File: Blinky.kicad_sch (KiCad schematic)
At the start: 34 parts, among them J1 DTF13-4P-G003, J2 Conn_01x01, J3 Conn_01x01, J4 Conn_01x01, Q1 IPD90P03P404ATMA2, Q2 IPD90P03P404ATMA2, U1 DCM4623TD2J13D0T70, U2 LTC3638xMSE

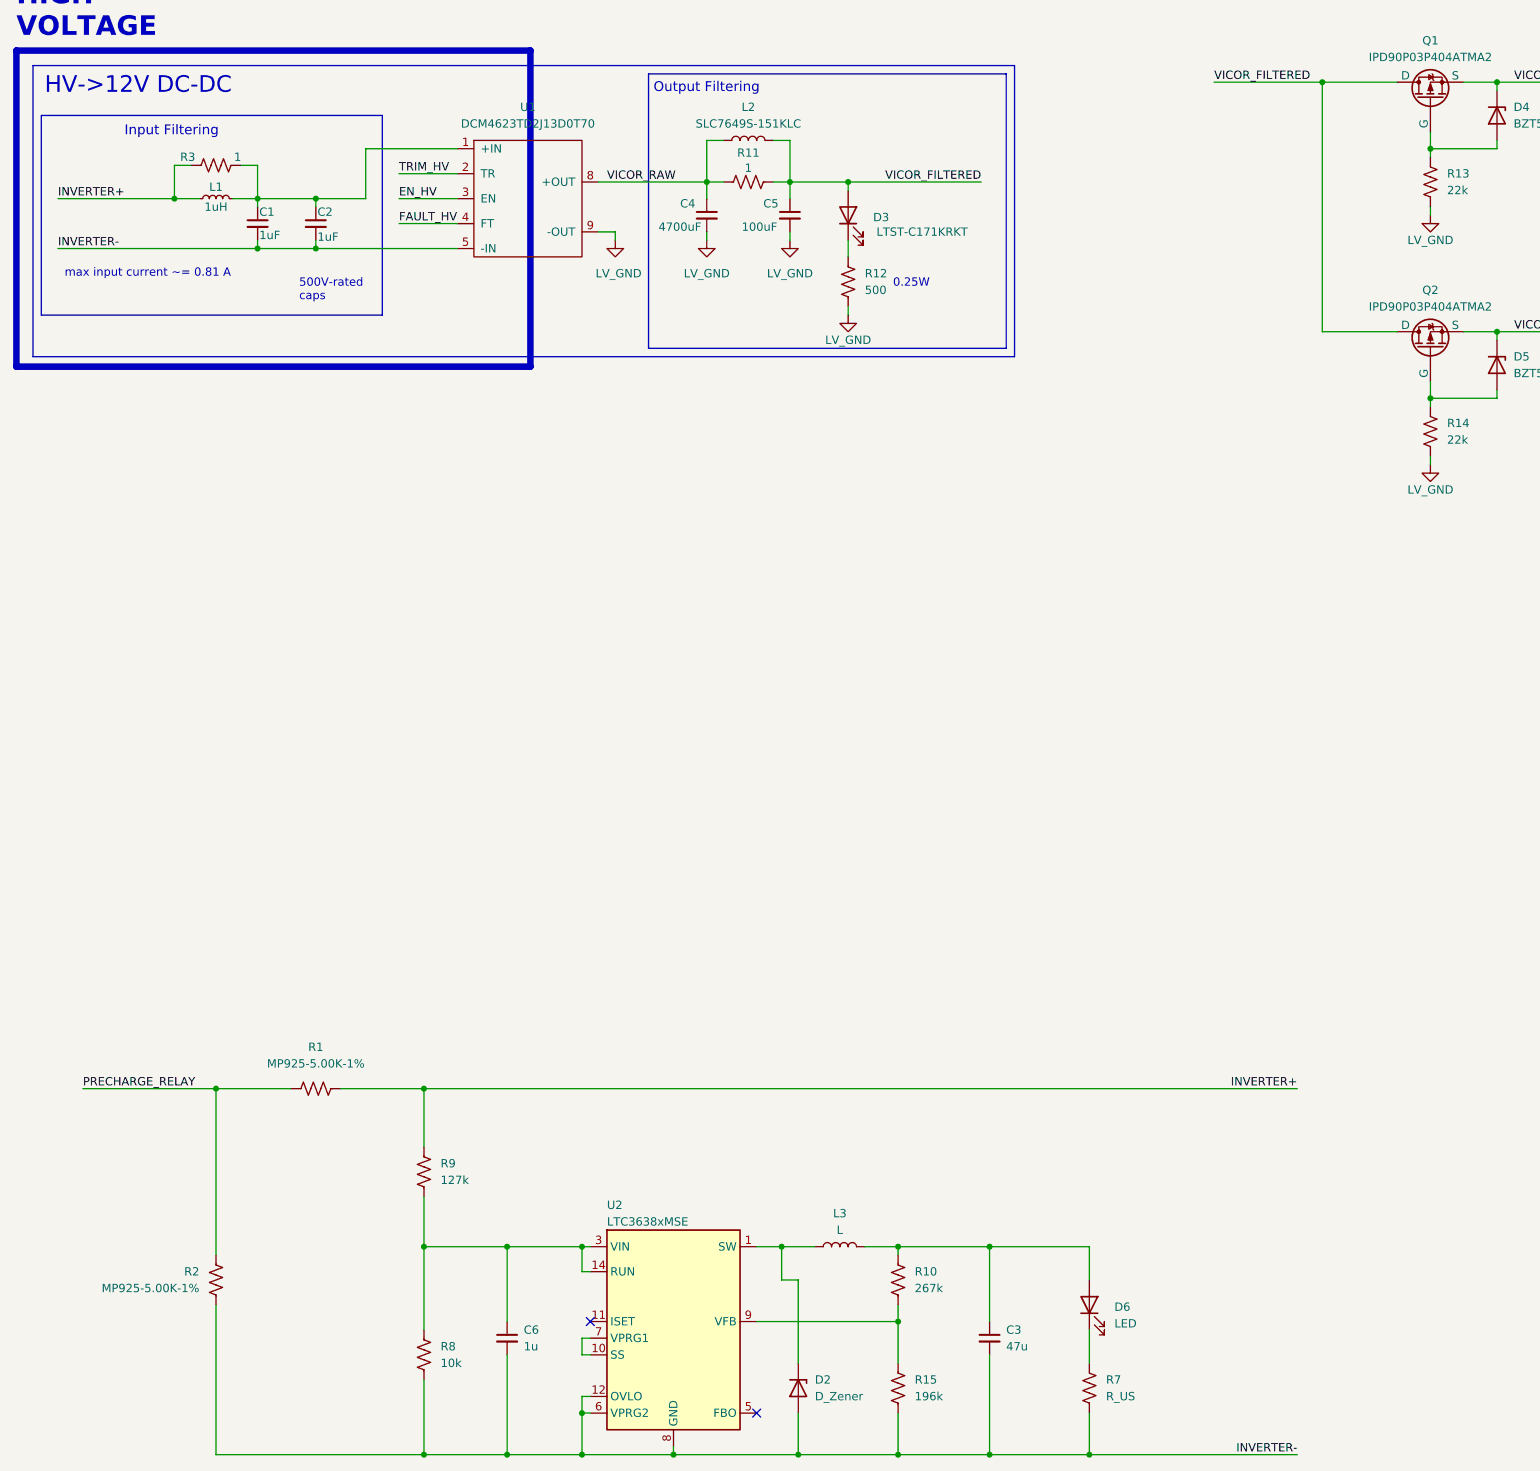
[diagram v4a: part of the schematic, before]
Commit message: further adjusted buck schematic
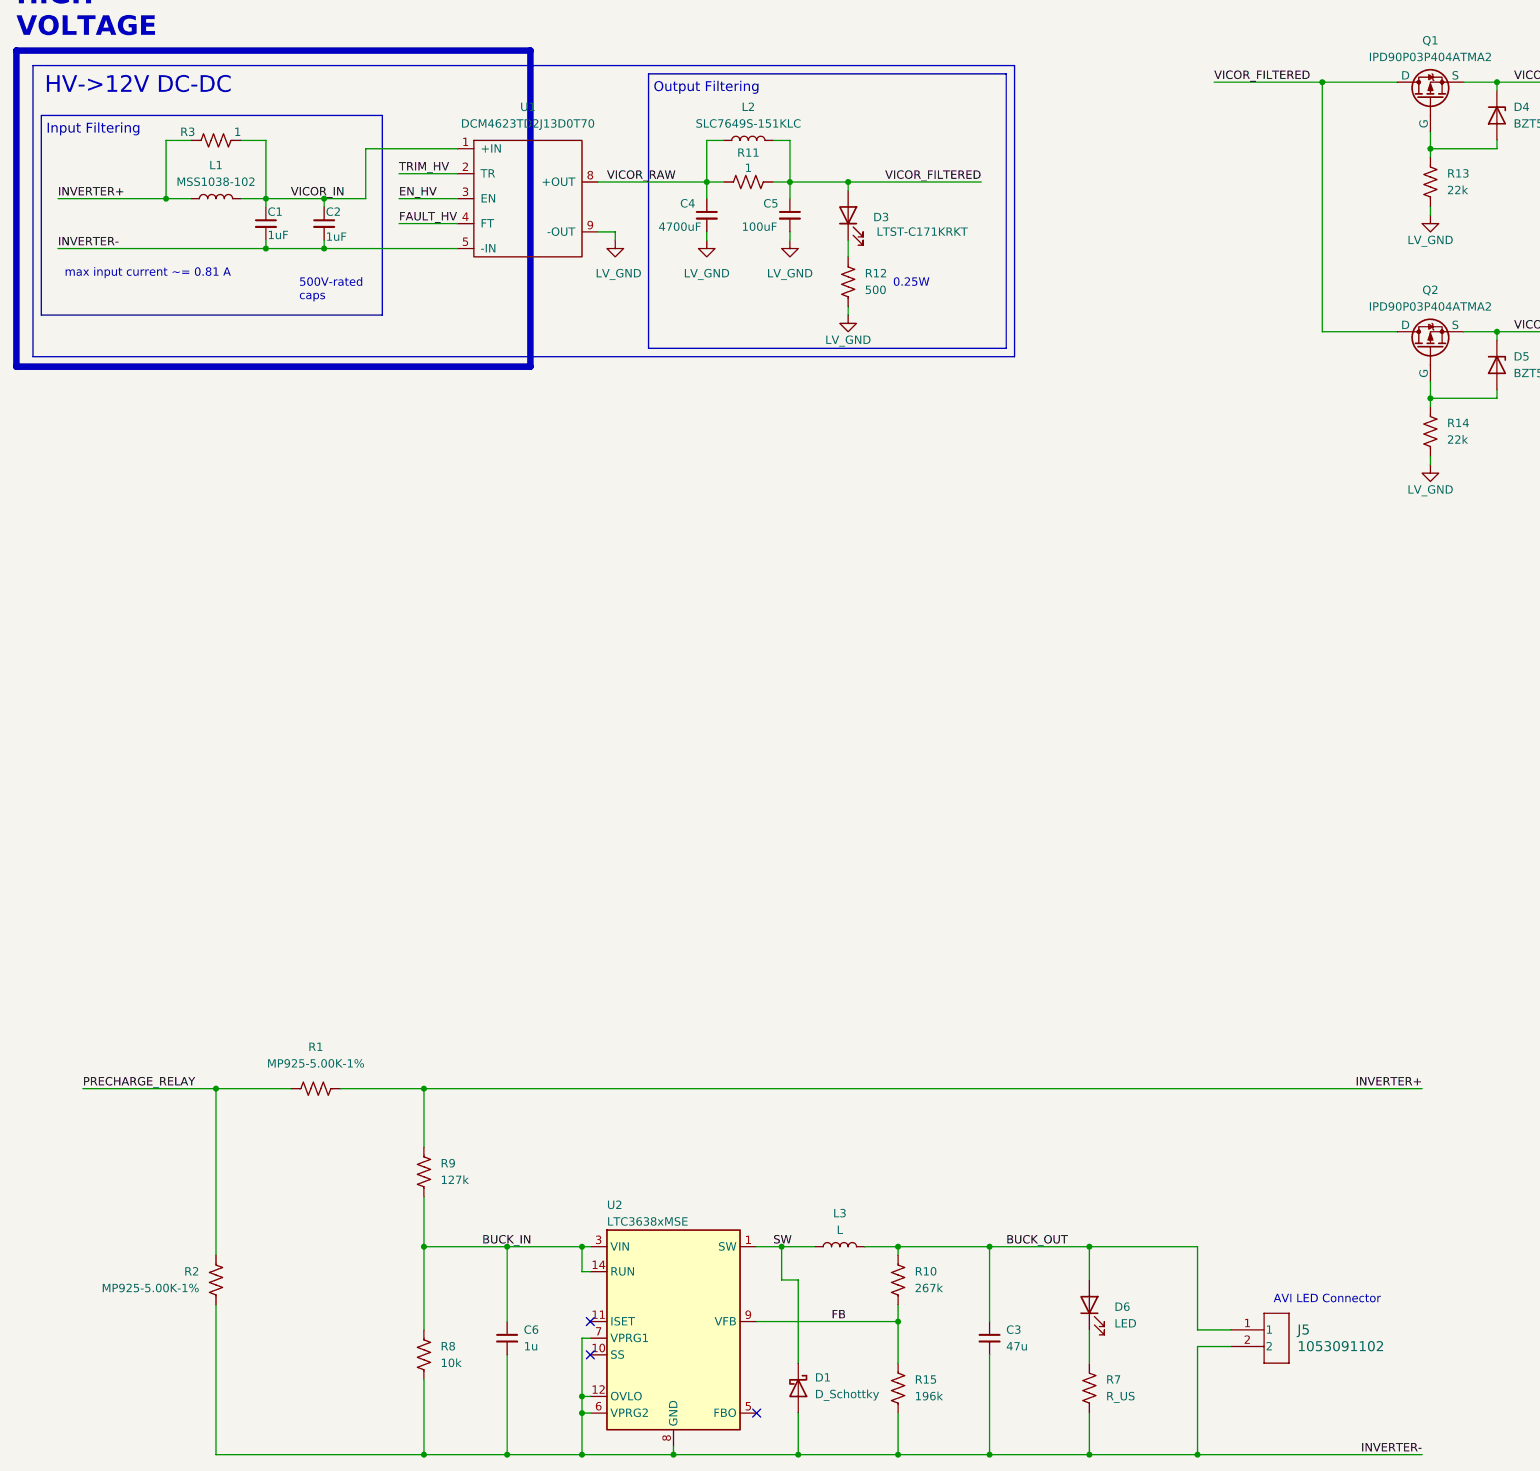
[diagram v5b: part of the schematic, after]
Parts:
- removed D2: D_Zener, symbol Device:D_Zener
- removed L1: 1uH, Inductor_SMD:L_1008_2520Metric_Pad1.43x2.20mm_HandSolder, symbol Device:L_Small
- added D1: D_Schottky, symbol Device:D_Schottky
- added J5: 1053091102, AERO_Connectors:1053091102, symbol AERO_Connectors:1053091102
- added L1: MSS1038-102, AERO_Inductors:MSS1038-102, symbol AERO_Inductors:MSS1038-102
- D6: footprint (none) -> LED_SMD:LED_0805_2012Metric_Pad1.15x1.40mm_HandSolder
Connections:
- net INVERTER+: now also L1.1
- net INVERTER-: now also U2.7 (VPRG1), D1.2 (A), J5.2
- net BUCK_IN: now reaches C6.1, R8.1, R9.2, U2.14 (RUN), U2.3 (VIN)
- net SW: now reaches L3.1, U2.1 (SW)
- net SW: now also D1.1 (K)
- net at U2.10 (SS): no longer U2.7 (VPRG1)
- net FB: now reaches R10.2, R15.1, U2.9 (VFB)
- net VICOR_IN: now reaches C1.1, C2.1, R3.1, U1.1 (+IN)
- net VICOR_IN: now also L1.2
- net BUCK_OUT: now reaches C3.1, D6.2 (A), L3.2, R10.1
- net BUCK_OUT: now also J5.1
- no-connect marks 2 -> 3
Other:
- note added: "AVI LED Connector"
- moved on the sheet: C1, C2, R3

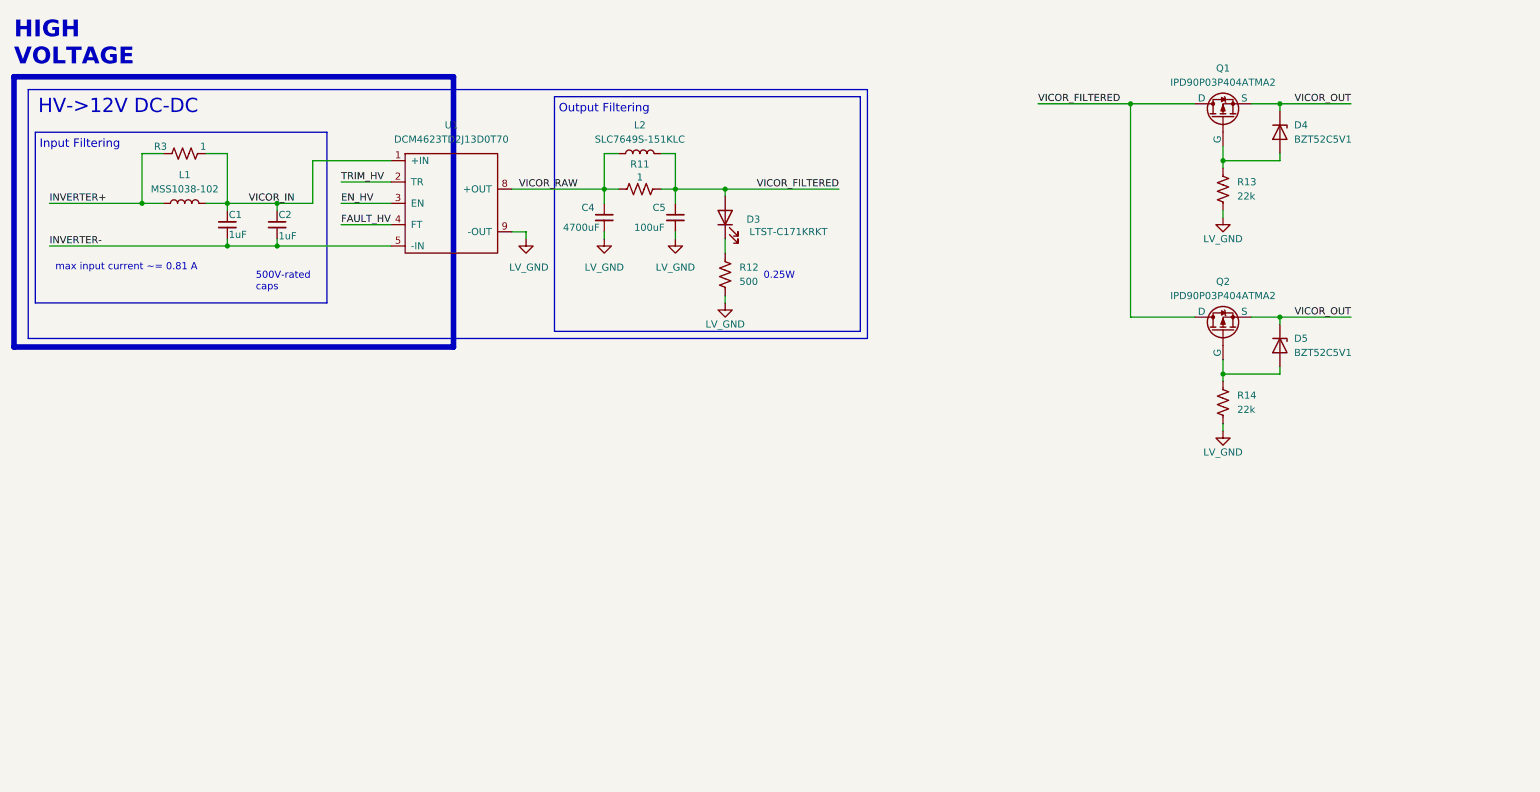
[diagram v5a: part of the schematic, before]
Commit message: added second VICOR
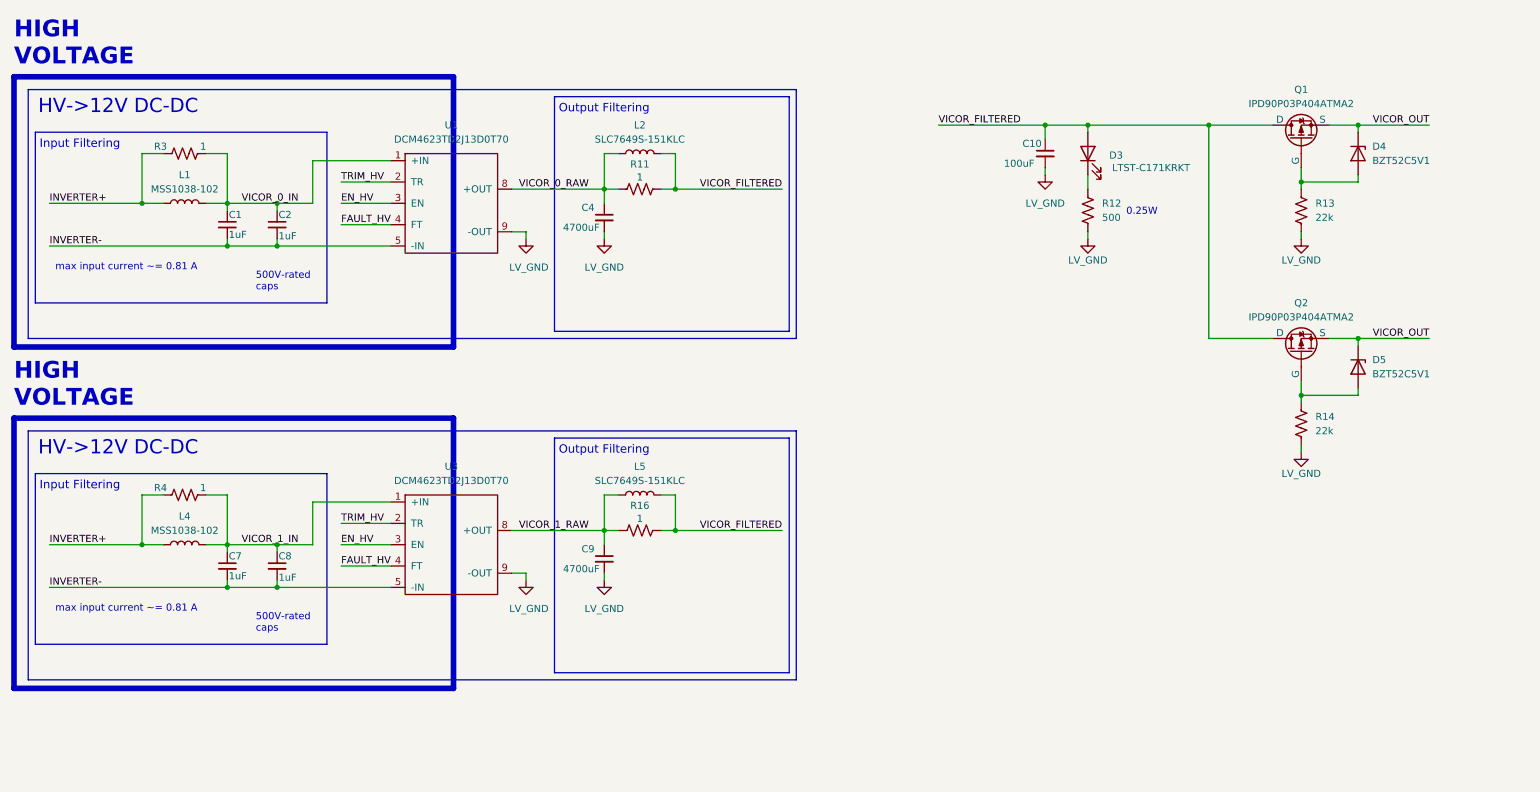
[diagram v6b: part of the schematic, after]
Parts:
- removed C5: 100uF, Capacitor_THT:C_Radial_D12.5mm_H25.0mm_P5.00mm, symbol Device:C_Small
- added C10: 100uF, Capacitor_THT:C_Radial_D12.5mm_H25.0mm_P5.00mm, symbol Device:C_Small
- added C7, C8: 1uF, Capacitor_THT:C_Rect_L18.0mm_W8.0mm_P15.00mm_FKS3_FKP3, symbol Device:C_Small
- added C9: 4700uF, Capacitor_THT:C_Radial_D12.5mm_H25.0mm_P5.00mm, symbol Device:C_Small
- added L4: MSS1038-102, AERO_Inductors:MSS1038-102, symbol AERO_Inductors:MSS1038-102
- added L5: SLC7649S-151KLC, AERO_Inductors:SLC7649S-151KLC, symbol AERO_Inductors:SLC7649S-151KLC
- added R16, R4: 1, Resistor_SMD:R_2512_6332Metric_Pad1.40x3.35mm_HandSolder, symbol Device:R_US
- added U3: DCM4623TD2J13D0T70, AERO_Regulators:DCM4623TD2J13D0T70, symbol AERO_Regulators:DCM4623TD2J13D0T70
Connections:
- net EN_HV: now also U3.3 (EN)
- net FAULT_HV: now also U3.4 (FT)
- net INVERTER+: now also L4.1, R4.2
- net INVERTER-: now also C7.2, C8.2, U3.5 (-IN)
- net LV_GND: now also C10.2, C9.2, U3.9 (-OUT)
- net TRIM_HV: now also U3.2 (TR)
- net VICOR_FILTERED: now also C10.1, L5.2, R16.1
- net VICOR_IN renamed VICOR_0_IN
- net VICOR_RAW renamed VICOR_0_RAW
- new net VICOR_1_IN: C7.1, C8.1, L4.2, R4.1, U3.1 (+IN)
- new net VICOR_1_RAW: C9.1, L5.1, R16.2, U3.8 (+OUT)
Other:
- moved on the sheet: D4, D5, Q1, Q2, R13, R14

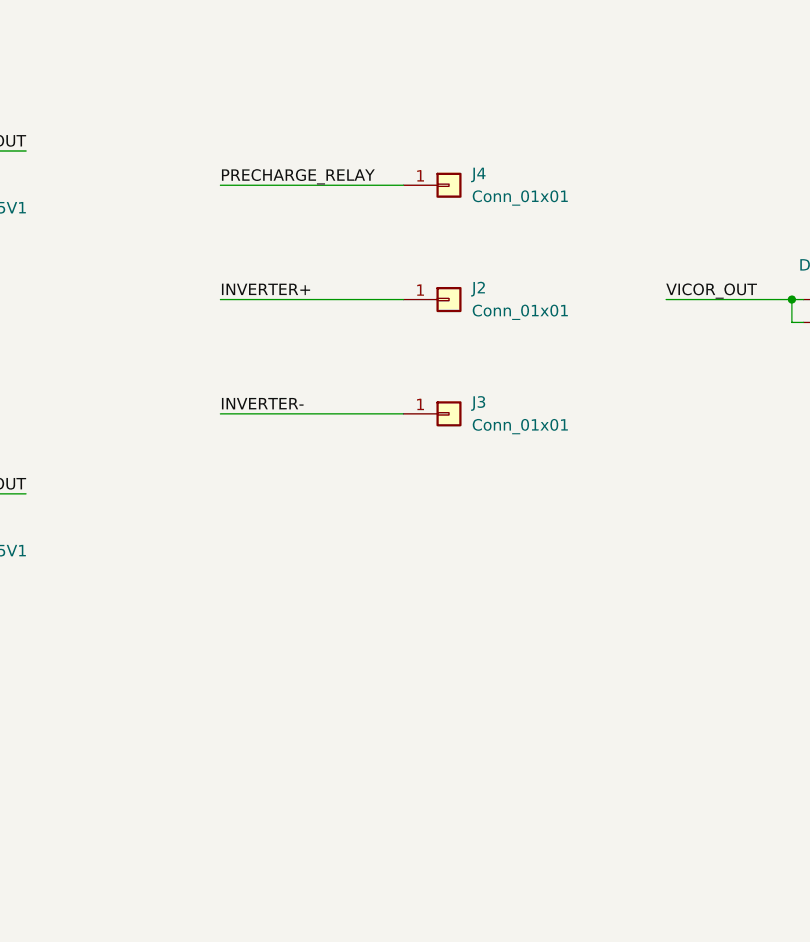
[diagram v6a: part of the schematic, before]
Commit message: added more connectors for HV board stuff
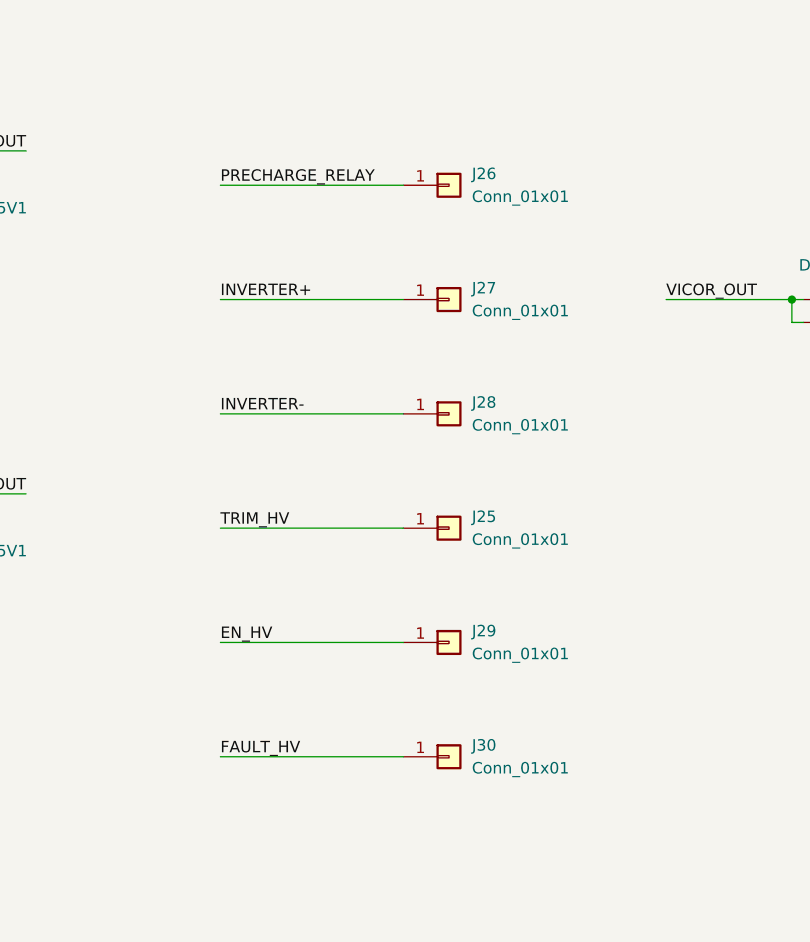
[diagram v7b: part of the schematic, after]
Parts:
- removed J2, J3, J4: Conn_01x01, symbol Connector_Generic:Conn_01x01
- added J25, J26, J27, J28, J29, J30: Conn_01x01, Connector_Hirose:Hirose_DF63M-1P-3.96DSA_1x01_P3.96mm_Vertical, symbol Connector_Generic:Conn_01x01
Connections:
- net EN_HV: now also J29.1 (Pin_1)
- net FAULT_HV: now also J30.1 (Pin_1)
- net INVERTER+: now also J27.1 (Pin_1)
- net INVERTER-: now also J28.1 (Pin_1)
- net PRECHARGE_RELAY: now also J26.1 (Pin_1)
- net TRIM_HV: now also J25.1 (Pin_1)
